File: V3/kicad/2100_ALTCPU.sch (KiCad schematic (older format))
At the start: 20 parts, among them U1 74HCT273, U2100 Z8-L180-S180-180-PQFP-80, U2101 GAL16V8, U2102 14.7456 MHz

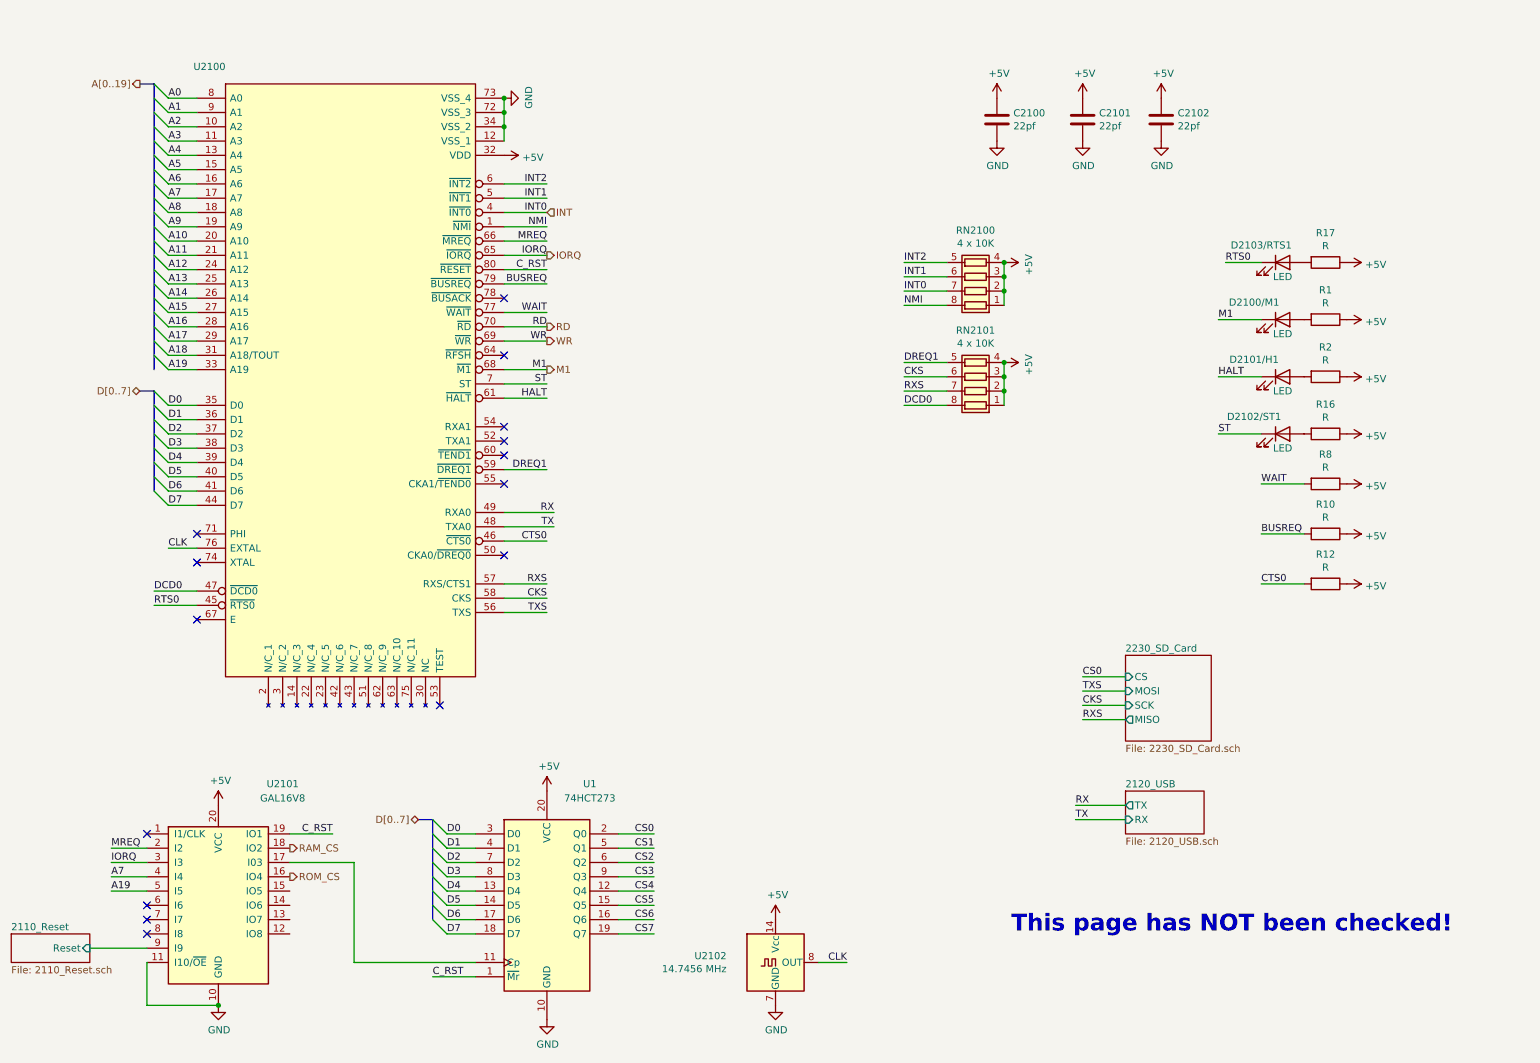
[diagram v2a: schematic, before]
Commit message: added cap for SPI FF
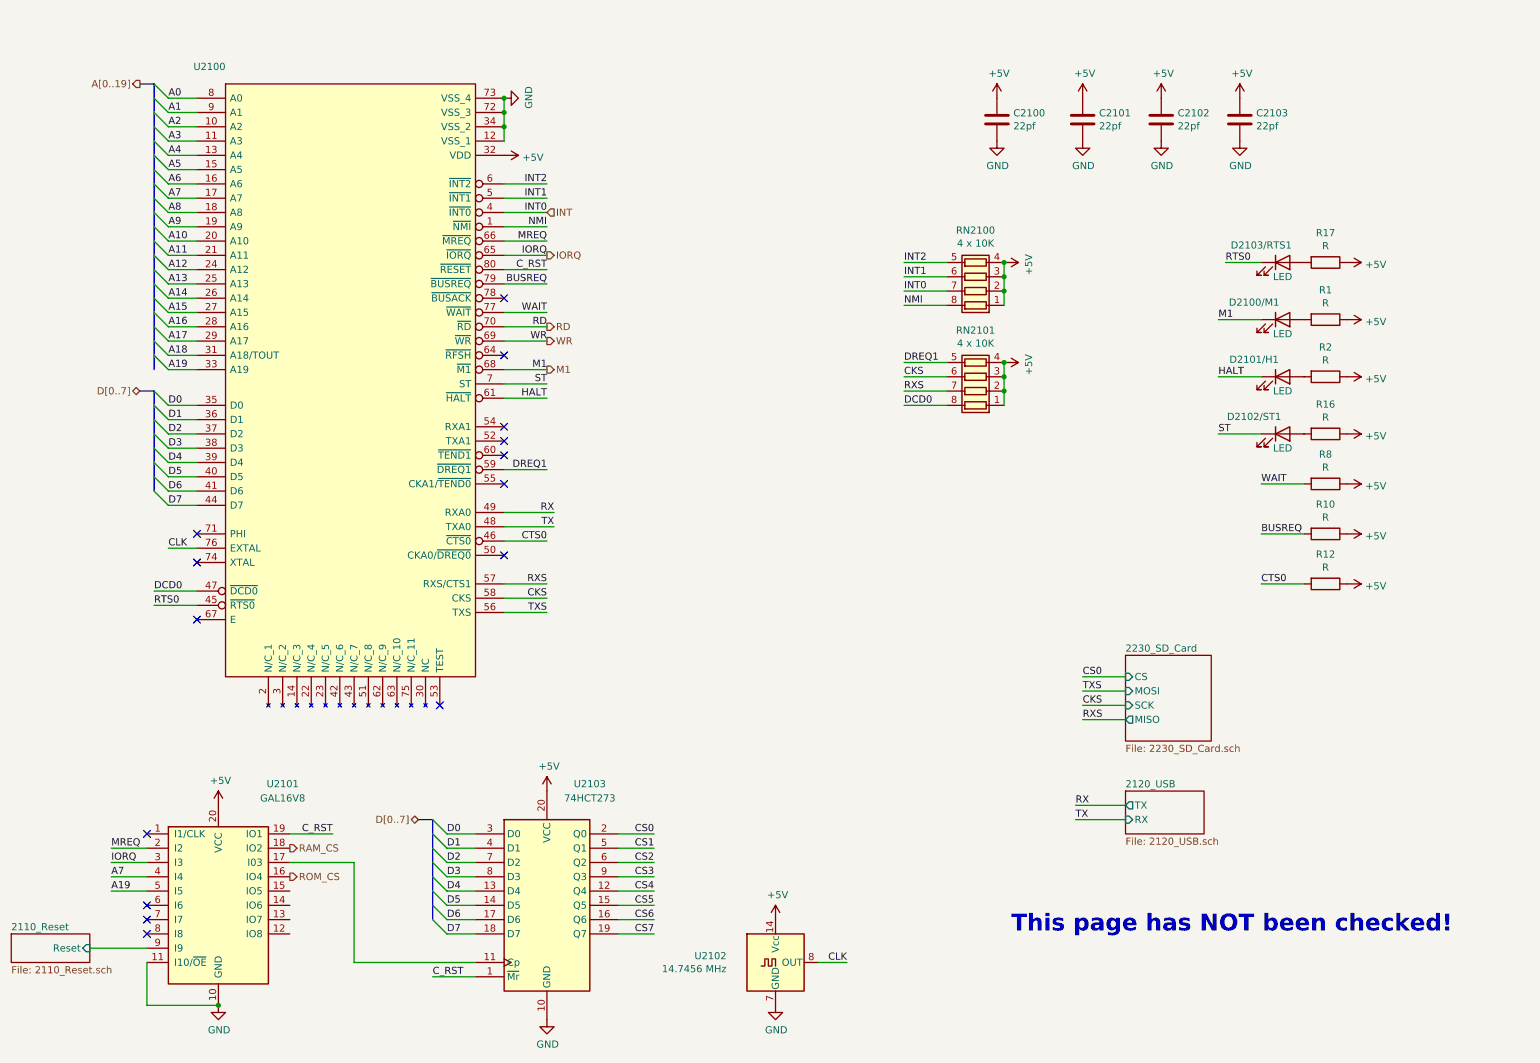
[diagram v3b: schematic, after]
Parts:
- added C2103: 22pf, Capacitor_SMD:C_1206_3216Metric, symbol Device:C
- renumbered U1 to U2103
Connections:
- net +5V: now also C2103.1
- net GND: now also C2103.2
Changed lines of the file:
@@
 TXS
 $Comp
-L 74xx:74HCT273 U1
+L 74xx:74HCT273 U2103
 U 1 1 63802B80
 P 4450 6750
-F 0 "U1" H 4750 7600 50  0000 C CNN
+F 0 "U2103" H 4750 7600 50  0000 C CNN
 F 1 "74HCT273" H 4750 7500 50  0000 C CNN
 F 2 "Package_SO:SOIC-20W_7.5x12.8mm_P1.27mm" H 4450 6750 50  0001 C CNN
@@
 Wire Wire Line
 	8200 5150 8500 5150
+$Comp
+L Device:C C?
+U 1 1 63A7CF83
+P 9300 1250
+AR Path="/6195D2C9/63A7CF83" Ref="C?"  Part="1"
+AR Path="/6191B6A2/61F28B7D/63A7CF83" Ref="C?"  Part="1"
+AR Path="/6191B6A2/61EBDADB/63A7CF83" Ref="C2103"  Part="1"
+F 0 "C2103" H 9415 1296 50  0000 L CNN
+F 1 "22pf" H 9415 1205 50  0000 L CNN
+F 2 "Capacitor_SMD:C_1206_3216Metric" H 9338 1100 50  0001 C CNN
+F 3 "~" H 9300 1250 50  0001 C CNN
+	1    9300 1250
+	1    0    0    -1
+$EndComp
+$Comp
+L power:GND #PWR?
+U 1 1 63A7CF89
+P 9300 1400
+AR Path="/63A7CF89" Ref="#PWR?"  Part="1"
+AR Path="/62497D60/63A7CF89" Ref="#PWR?"  Part="1"
+AR Path="/61D852D7/63A7CF89" Ref="#PWR?"  Part="1"
+AR Path="/6195D2C9/63A7CF89" Ref="#PWR?"  Part="1"
+AR Path="/6191B6A2/61F28B7D/63A7CF89" Ref="#PWR?"  Part="1"
+AR Path="/6191B6A2/61EBDADB/63A7CF89" Ref="#PWR?"  Part="1"
+F 0 "#PWR?" H 9300 1150 50  0001 C CNN
+F 1 "GND" H 9305 1227 50  0000 C CNN
+F 2 "" H 9300 1400 50  0001 C CNN
+F 3 "" H 9300 1400 50  0001 C CNN
+	1    9300 1400
+	1    0    0    -1
+$EndComp
+$Comp
+L power:+5V #PWR?
+U 1 1 63A7CF8F
+P 9300 1100
+AR Path="/6195D2C9/63A7CF8F" Ref="#PWR?"  Part="1"
+AR Path="/6191B6A2/61F28B7D/63A7CF8F" Ref="#PWR?"  Part="1"
+AR Path="/6191B6A2/61EBDADB/63A7CF8F" Ref="#PWR?"  Part="1"
+F 0 "#PWR?" H 9300 950 50  0001 C CNN
+F 1 "+5V" H 9315 1273 50  0000 C CNN
+F 2 "" H 9300 1100 50  0001 C CNN
+F 3 "" H 9300 1100 50  0001 C CNN
+	1    9300 1100
+	1    0    0    -1
+$EndComp
 Wire Bus Line
 	1700 3150 1700 3850
